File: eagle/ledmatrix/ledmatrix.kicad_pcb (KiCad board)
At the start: 2 copper layers, 21 parts, among them P1 CONN_01X05, Q1 BSS138, U1 74HC595, U2 74HC595, U3 74HC595

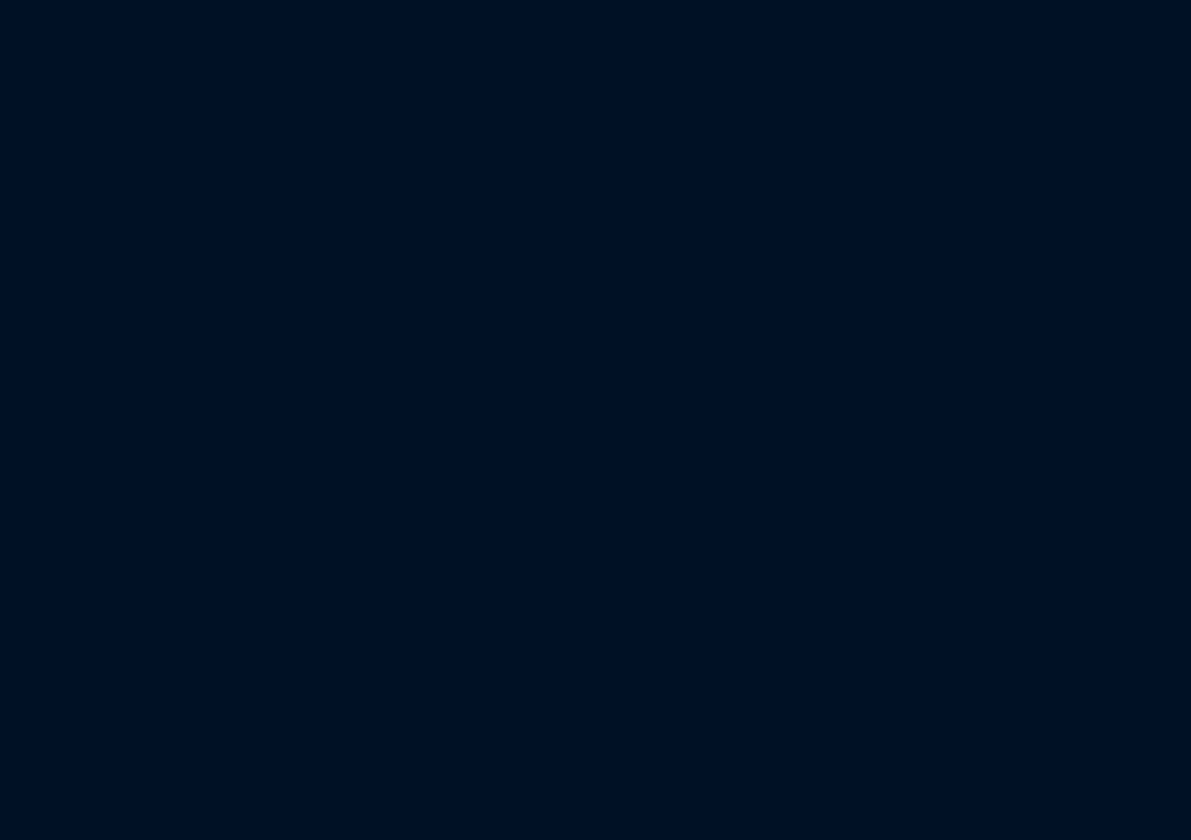
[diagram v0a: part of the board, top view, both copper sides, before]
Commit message: continue work on the ledmatrix schematic and board.
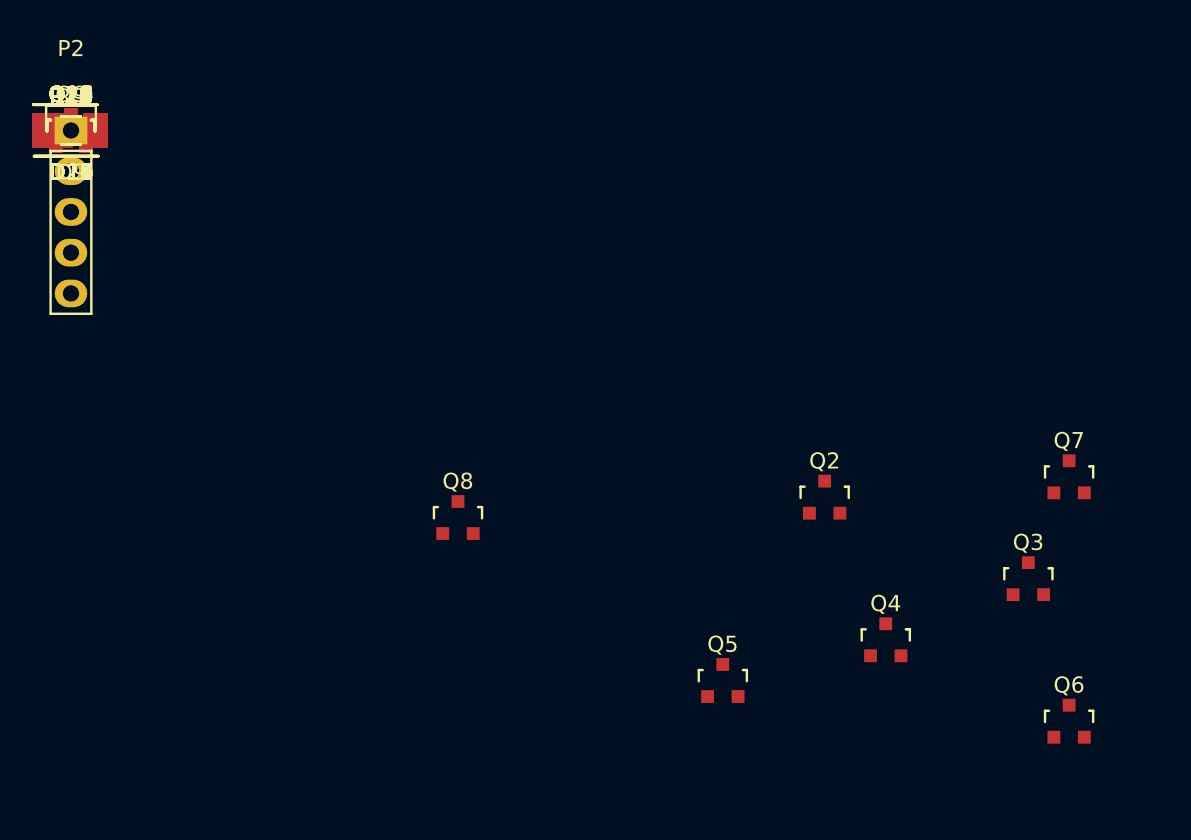
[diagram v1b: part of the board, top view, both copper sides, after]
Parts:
- added D10, D11, D12, D13, D14, D15, D16, D17, D18, D19, D20, D9: LED, LEDs:LED_PLCC_2835_Handsoldering, F.Cu at (0.00, 0.00)
- added P2: CONN_01X05, Pin_Headers:Pin_Header_Straight_1x05, F.Cu at (0.00, 0.00)
- added Q10, Q11, Q12, Q13, Q14, Q15, Q16, Q17, Q18, Q19, Q20, Q9: BSS138, TO_SOT_Packages_SMD:SOT-23, F.Cu at (0.00, 0.00)
- added Q2: BSS138, TO_SOT_Packages_SMD:SOT-23, F.Cu at (47.0, 22.9)
- added Q3: BSS138, TO_SOT_Packages_SMD:SOT-23, F.Cu at (59.7, 27.9)
- added Q4: BSS138, TO_SOT_Packages_SMD:SOT-23, F.Cu at (50.8, 31.8)
- added Q5: BSS138, TO_SOT_Packages_SMD:SOT-23, F.Cu at (40.6, 34.3)
- added Q6: BSS138, TO_SOT_Packages_SMD:SOT-23, F.Cu at (62.2, 36.8)
- added Q7: BSS138, TO_SOT_Packages_SMD:SOT-23, F.Cu at (62.2, 21.6)
- added Q8: BSS138, TO_SOT_Packages_SMD:SOT-23, F.Cu at (24.1, 24.1)
- added R10, R11, R12, R13, R14, R15, R16, R17, R18, R19, R20, R9: R, Resistors_SMD:R_0805_HandSoldering, F.Cu at (0.00, 0.00)
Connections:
- D1 pad 2: Net-(D1-Pad2) -> +5V
- D2 pad 2: Net-(D2-Pad2) -> +5V
- D3 pad 2: Net-(D3-Pad2) -> +5V
- D4 pad 2: Net-(D4-Pad2) -> +5V
- D5 pad 2: Net-(D5-Pad2) -> +5V
- D6 pad 2: Net-(D6-Pad2) -> +5V
- D7 pad 2: Net-(D7-Pad2) -> +5V
- D8 pad 2: Net-(D8-Pad2) -> +5V
- P1 pad 4: VCC -> +5V
- R1 pad 2: Net-(R1-Pad2) -> Net-(Q1-Pad3)
- U1 pad 10: Net-(U1-Pad10) -> +5V
- U1 pad 13: Net-(U1-Pad13) -> GND
- U1 pad 16: VCC -> +5V
- U2 pad 10: Net-(U2-Pad10) -> +5V
- U2 pad 13: Net-(U2-Pad13) -> GND
- U2 pad 16: VCC -> +5V
- U3 pad 10: Net-(U3-Pad10) -> +5V
- U3 pad 13: Net-(U3-Pad13) -> GND
- U3 pad 16: VCC -> +5V

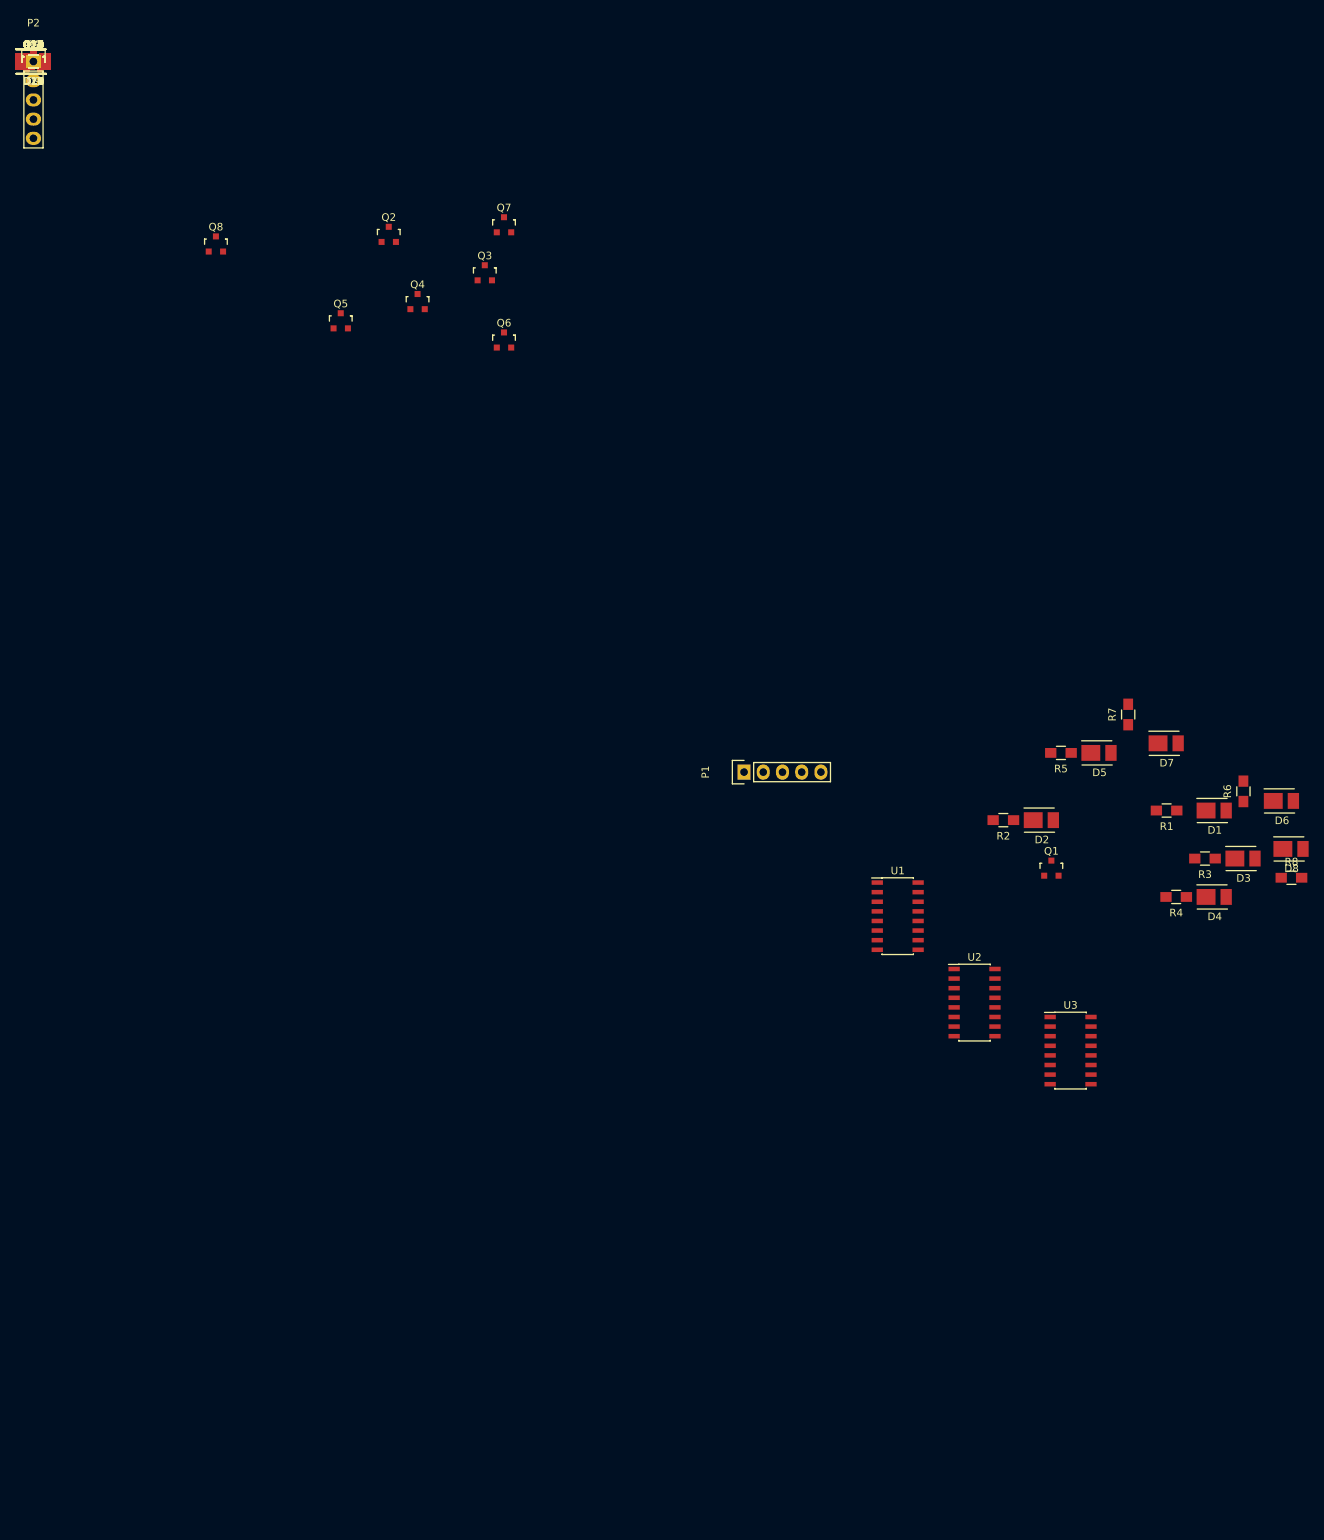
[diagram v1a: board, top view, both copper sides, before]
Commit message: layout components.
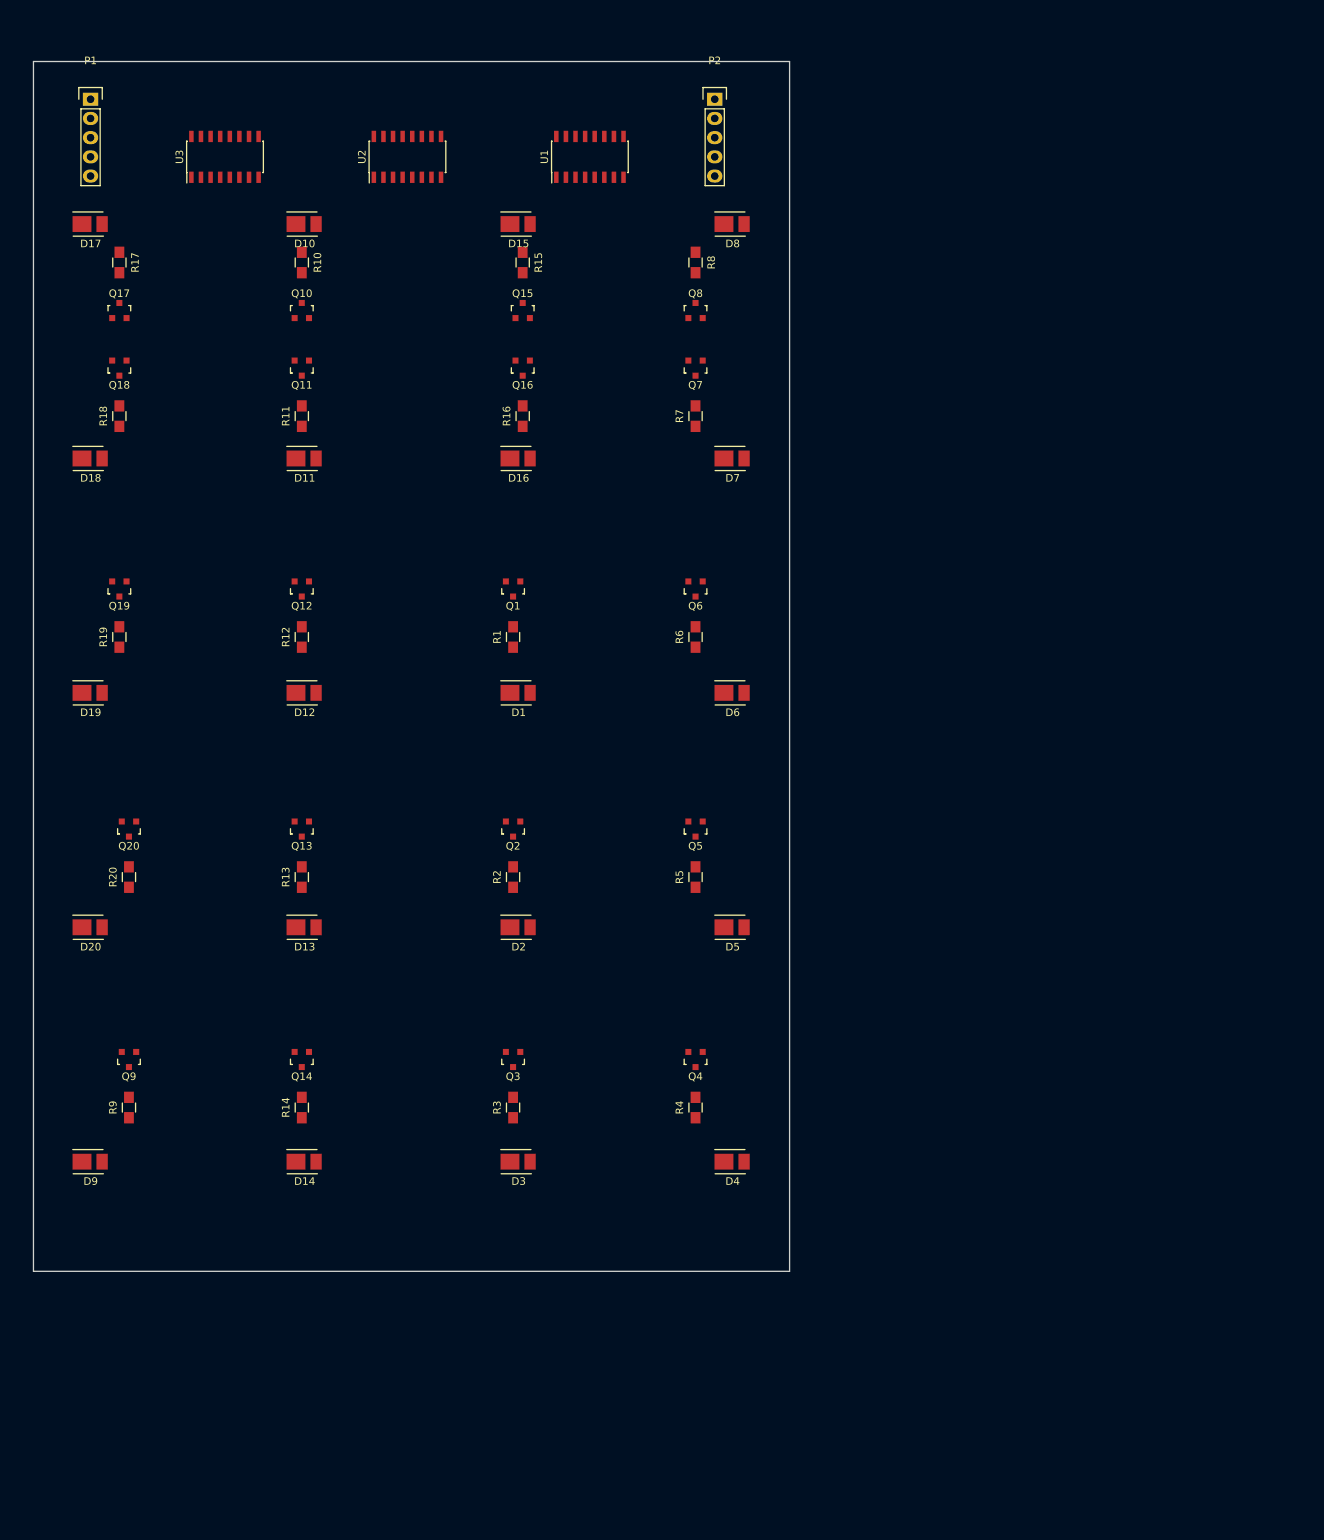
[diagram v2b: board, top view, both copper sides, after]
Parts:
- moved U3 162.7 mm to (25.3, 12.6), turned to 90 degrees
- moved D14 149.9 mm to (35.9, 145.5)
- moved D9 145.7 mm to (7.55, 145.5)
- moved R14 142.8 mm to (35.5, 138.3), turned to 90 degrees
- moved R9 138.9 mm to (12.6, 138.3), turned to 90 degrees
- moved Q14 136.7 mm to (35.5, 132.0), turned to 180 degrees
- moved U2 134.7 mm to (49.5, 12.6), turned to 90 degrees
- moved Q9 132.6 mm to (12.6, 132.0), turned to 180 degrees
- moved P1 124.1 mm to (7.55, 4.99), turned to 0 degrees
- moved D13 120.0 mm to (35.9, 114.5)
- moved D20 114.7 mm to (7.55, 114.5)
- moved R13 113.5 mm to (35.5, 107.9), turned to 90 degrees
- moved R8 113.3 mm to (87.6, 26.6), turned to 270 degrees
- moved D8 110.9 mm to (92.5, 21.5)
- moved R20 108.6 mm to (12.6, 107.9), turned to 90 degrees
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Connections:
- U2 pad 15: Net-(Q9-Pad1) -> Net-(U2-Pad15)
- U2 pad 6: Net-(Q15-Pad1) -> Net-(Q16-Pad1)
- U2 pad 7: Net-(Q16-Pad1) -> Net-(Q15-Pad1)
- U3 pad 4: Net-(U3-Pad4) -> Net-(Q9-Pad1)
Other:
- board outline added: 100 x 160 mm

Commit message: more routing -- latch, clock proposal 1
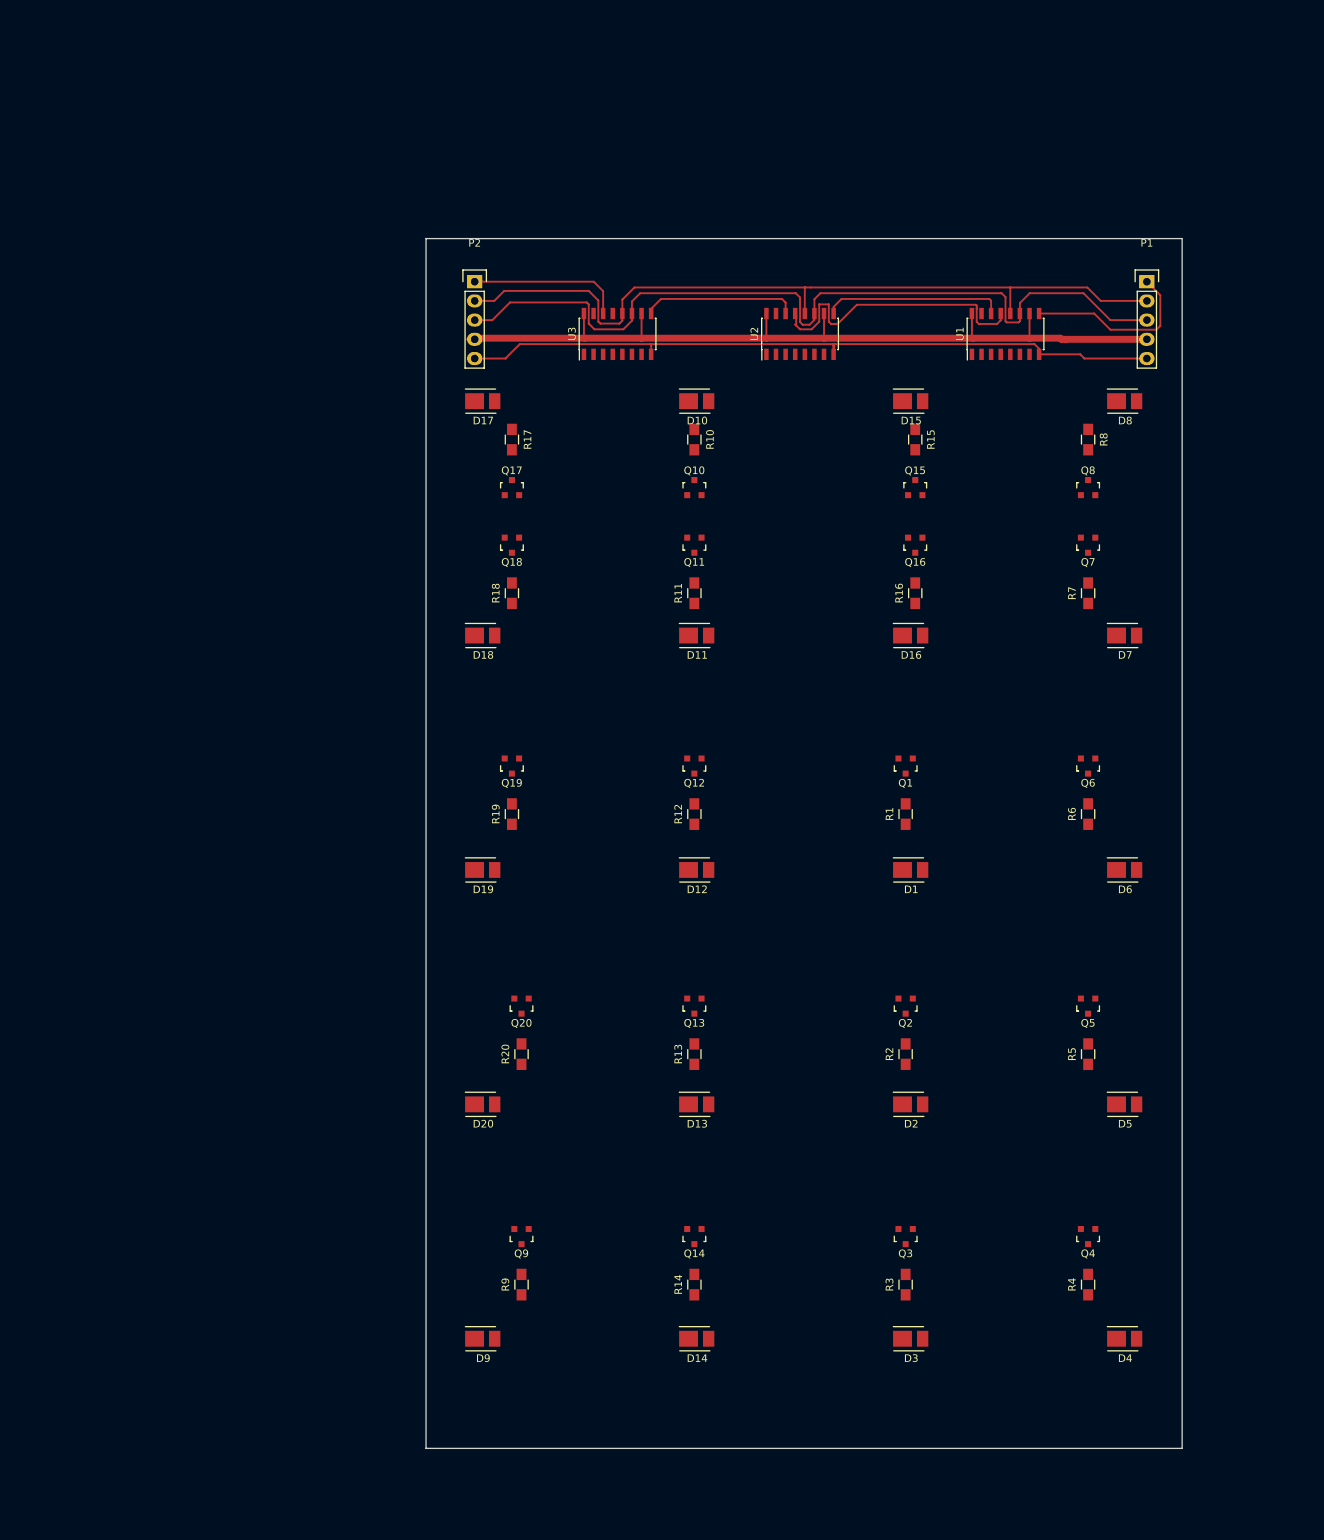
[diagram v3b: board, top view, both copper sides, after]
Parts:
- moved P1 141.8 mm to (147.3, 29.1)
- moved U1 59.7 mm to (128.6, 36.0)
- moved D1 57.0 mm to (116.1, 106.9)
- moved D16 57.0 mm to (116.1, 75.9)
- moved D2 57.0 mm to (116.1, 137.9)
- moved D3 57.0 mm to (116.1, 168.9)
- moved D4 57.0 mm to (144.4, 168.9)
- moved D5 57.0 mm to (144.4, 137.9)
- moved D6 57.0 mm to (144.4, 106.9)
- moved D7 57.0 mm to (144.4, 75.9)
- moved D8 57.0 mm to (144.4, 44.9)
- moved Q15 57.0 mm to (116.6, 56.3)
- moved Q16 57.0 mm to (116.6, 64.0)
- moved Q4 57.0 mm to (139.5, 155.4)
- moved Q5 57.0 mm to (139.5, 124.9)
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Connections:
- net Net-(P1-Pad2) renamed /latch
- net Net-(P1-Pad3) renamed /clk
- P1 pad 1: Net-(P1-Pad1) -> /ser_out
- P2 pad 1: Net-(P2-Pad1) -> /ser_in
- U1 pad 14: Net-(P1-Pad1) -> /casc_u2u1
- U1 pad 15: Net-(Q1-Pad1) -> Net-(U1-Pad15)
- U1 pad 9: Net-(U1-Pad9) -> /ser_out
- U2 pad 14: Net-(U1-Pad9) -> /casc_u3u2
- U2 pad 5: Net-(Q14-Pad1) -> Net-(Q1-Pad1)
- U2 pad 9: Net-(U2-Pad9) -> /casc_u2u1
- U3 pad 1: Net-(Q18-Pad1) -> Net-(Q17-Pad1)
- U3 pad 14: Net-(U2-Pad9) -> /ser_in
- U3 pad 15: Net-(Q17-Pad1) -> Net-(U3-Pad15)
- U3 pad 2: Net-(Q19-Pad1) -> Net-(Q18-Pad1)
- U3 pad 3: Net-(Q20-Pad1) -> Net-(Q19-Pad1)
- U3 pad 4: Net-(Q9-Pad1) -> Net-(Q20-Pad1)
- U3 pad 5: Net-(U3-Pad5) -> Net-(Q9-Pad1)
- U3 pad 6: Net-(U3-Pad6) -> Net-(Q14-Pad1)
- U3 pad 9: Net-(P2-Pad1) -> /casc_u3u2
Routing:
- net GND: track 0.00 -> 133.9 mm
- net +5V: track 0.00 -> 112.1 mm
- net /clk: track 0.00 -> 111.2 mm
- net /latch: track 0.00 -> 104.2 mm
- net /casc_u2u1: track 0.00 -> 23.9 mm
- net /ser_out: track 0.00 -> 23.7 mm
- net /casc_u3u2: track 0.00 -> 20.6 mm
- net /ser_in: track 0.00 -> 20.5 mm
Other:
- net class pwr added: clearance 0.4064, trace_width 0.508, via_dia 0.6, via_drill 0.4
- net class trk-freerange added: clearance 0.4064, trace_width 0.3048, via_dia 0.6, via_drill 0.4

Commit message: all routed
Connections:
- P1 pad 1: /ser_out -> /latch
- P1 pad 2: /latch -> /clk
- P1 pad 3: /clk -> /ser_out
- P2 pad 1: /ser_in -> /latch
- P2 pad 2: /latch -> /clk
- P2 pad 3: /clk -> /ser_in
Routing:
- net GND: track 133.9 -> 1041.4 mm
- net +5V: track 112.1 -> 856.4 mm
- net Net-(Q4-Pad1): track 0.00 -> 121.4 mm
- net Net-(Q9-Pad1): track 0.00 -> 120.8 mm
- net Net-(Q14-Pad1): track 0.00 -> 120.2 mm
- net Net-(Q3-Pad1): track 0.00 -> 119.4 mm
- net Net-(Q5-Pad1): track 0.00 -> 90.4 mm
- net Net-(Q13-Pad1): track 0.00 -> 90.3 mm
- net Net-(Q20-Pad1): track 0.00 -> 89.8 mm
- net Net-(Q2-Pad1): track 0.00 -> 88.4 mm
- net Net-(Q1-Pad1): track 0.00 -> 59.4 mm
- net Net-(Q6-Pad1): track 0.00 -> 58.1 mm
- net Net-(Q19-Pad1): track 0.00 -> 58.1 mm
- net Net-(Q12-Pad1): track 0.00 -> 58.1 mm
- net Net-(Q16-Pad1): track 0.00 -> 31.6 mm
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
